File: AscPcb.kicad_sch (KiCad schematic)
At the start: 30 parts, among them J1 USB_C_Receptacle_USB2.0_16P, J2 B2B-PH-K-S, SW1 RESET, SW2 BOOT, U1 TLV75801PDRV, U2 BQ24040DSQR, U3 ESP32-C3-WROOM-02

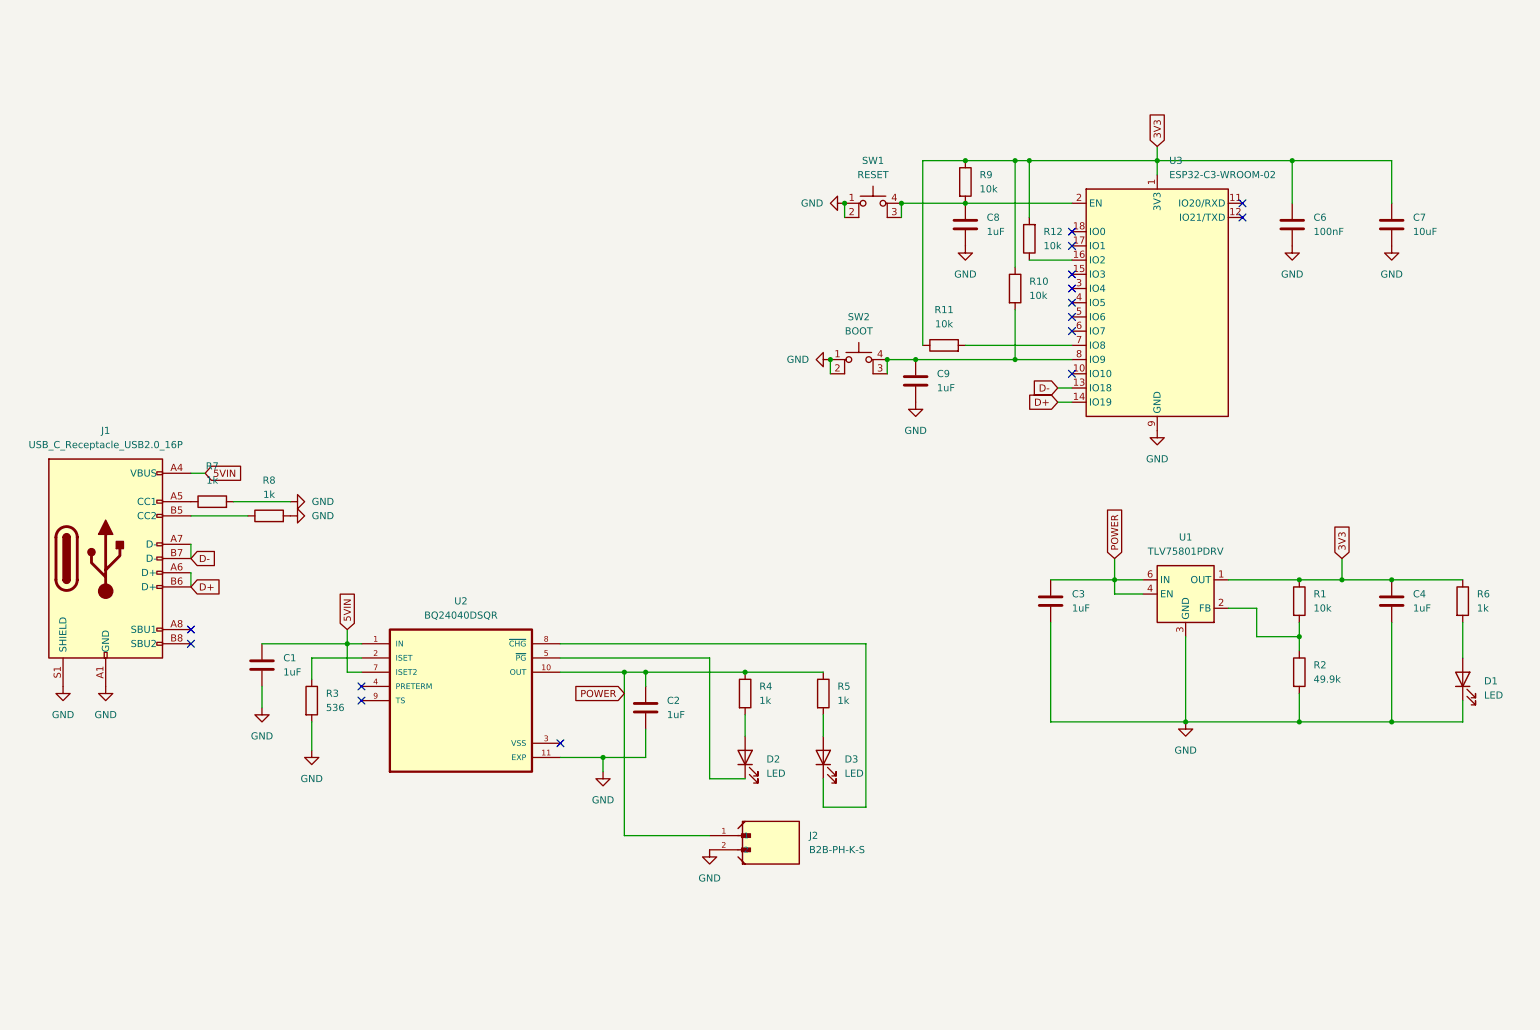
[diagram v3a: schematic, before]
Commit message: add more actual parts and add datasheets and MPNs
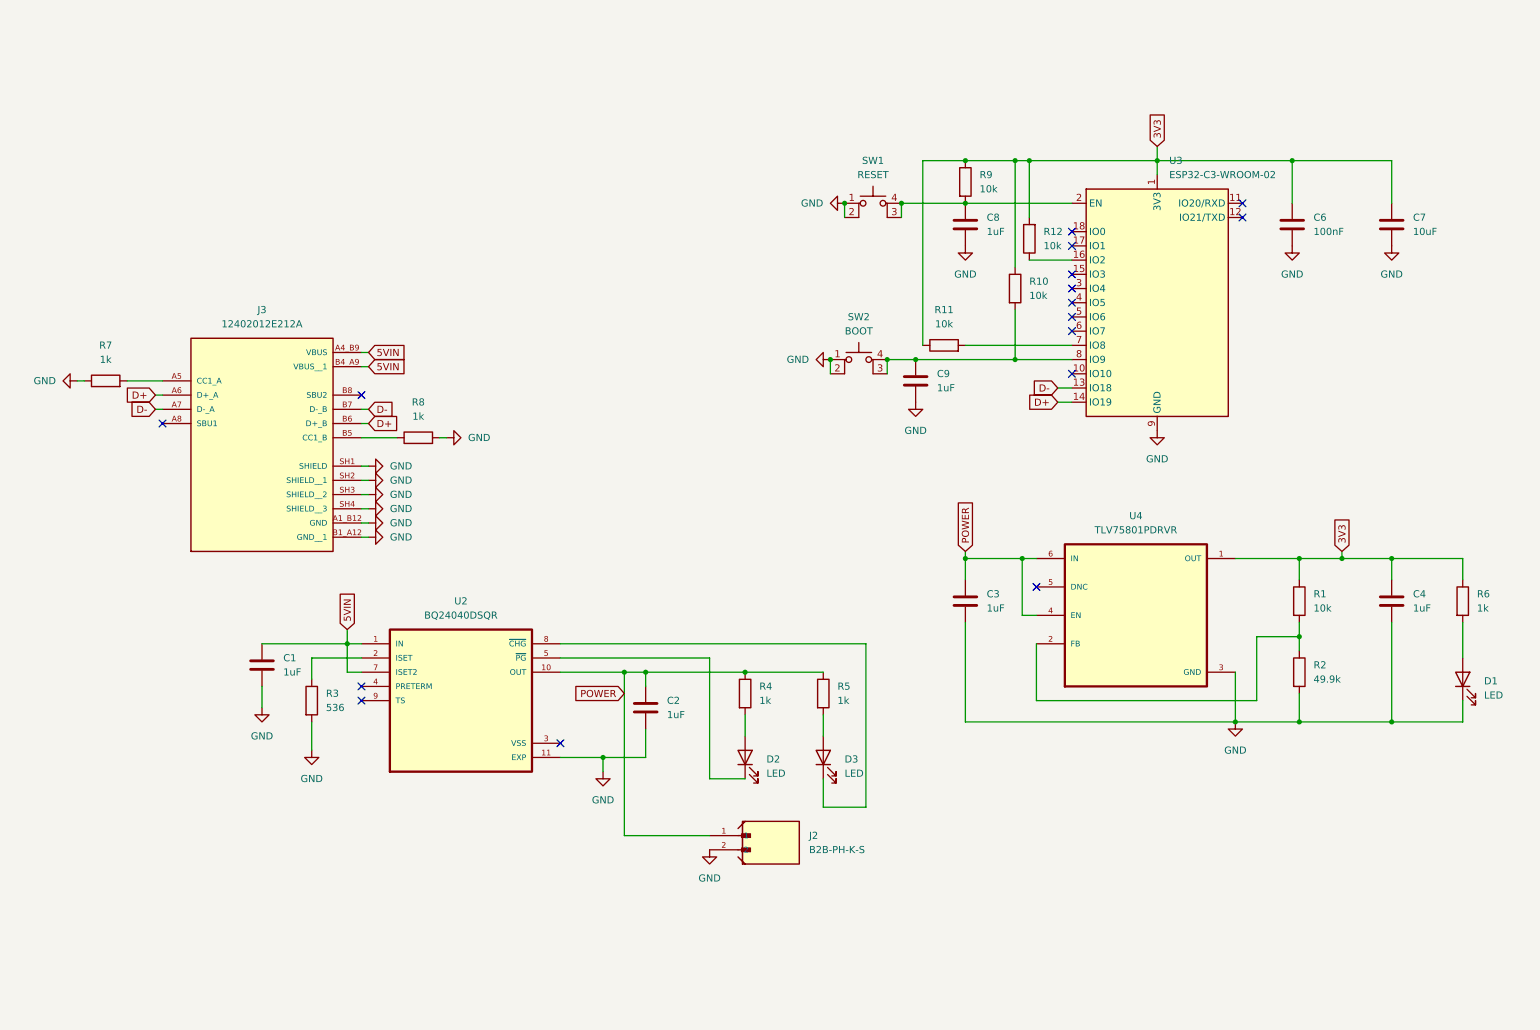
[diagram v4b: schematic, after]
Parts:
- removed J1: USB_C_Receptacle_USB2.0_16P, symbol Connector:USB_C_Receptacle_USB2.0_16P
- removed U1: TLV75801PDRV, Package_SON:WSON-6-1EP_2x2mm_P0.65mm_EP1x1.6mm, symbol Regulator_Linear:TLV75801PDRV
- added J3: 12402012E212A, 12402012E212A:AMPHENOL_12402012E212A, symbol 12402012E212A:12402012E212A
- added U4: TLV75801PDRVR, TLV75801PDRVR:SON65P200X200X80-7N, symbol TLV75801PDRVR:TLV75801PDRVR
- J2: MPN (none) -> B2B-PH-K-S
- U2: MPN (none) -> BQ24040DSQR
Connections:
- net 3V3: now also U4.1 (OUT)
- net 5VIN: now also J3.A4_B9 (VBUS), J3.B4_A9 (VBUS__1)
- net D+: now also J3.A6 (D+_A), J3.B6 (D+_B)
- net D-: now also J3.A7 (D-_A), J3.B7 (D-_B)
- net GND: now also R7.1, J3.A1_B12 (GND), J3.B1_A12 (GND__1), J3.SH1 (SHIELD), J3.SH2 (SHIELD__1), J3.SH3 (SHIELD__2), J3.SH4 (SHIELD__3), U4.3 (GND); no longer R7.2
- net POWER: now also U4.4 (EN), U4.6 (IN)
- net at R1.2, R2.1: now also U4.2 (FB)
- net at R8.1: now also J3.B5 (CC1_B)
- new net: J3.A5 (CC1_A), R7.2
- no-connect marks 15 -> 16
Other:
- moved on the sheet: C3

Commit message: clean up and other stuff
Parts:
- renumbered C6 to C5, C7 to C6, C8 to C7, C9 to C8, R7 to R1, R8 to R2, U3 to U1, U4 to U3
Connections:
- net 3V3 renamed +3V3
- net 5VIN renamed +5V
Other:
- moved on the sheet: C5, C6

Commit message: LEDs with correct Resistors
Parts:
- removed R6: 1k, Resistor_SMD:R_0603_1608Metric, symbol Device:R
- added R8: 30, Resistor_SMD:R_0603_1608Metric, symbol Device:R
- D1, D2: value LED -> Green; MPN (none) -> L135-R625003500001
- D3: value LED -> RED; MPN (none) -> L135-G525003500000
- R4, R5: value 1k -> 30; MPN CRCW06031K00FKEA -> RCP0603B30R0GEA
- renumbered R1 to R6, R2 to R7
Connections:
- net +3V3: now also R8.1
- net at D1.2 (A): now also R8.2

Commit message: schematic done
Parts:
- removed D1, D2: Green, LED_SMD:LED_0603_1608Metric, symbol Device:LED
- removed D3: RED, LED_SMD:LED_0603_1608Metric, symbol Device:LED
- removed SW1: RESET, Button_Switch_SMD:SW_SPST_PTS810, symbol Switch:SW_MEC_5E
- removed SW2: BOOT, Button_Switch_SMD:SW_SPST_PTS810, symbol Switch:SW_MEC_5E
- added D2: RED, L135_G525003500000:LED_L135-G525003500000, symbol L135-G525003500000:L135-G525003500000
- added D3, D4: Green, L135_G525003500000:LED_L135-G525003500000, symbol L135-G525003500000:L135-G525003500000
- added J3: Conn_01x10_Pin, Connector_PinHeader_1.00mm:PinHeader_1x10_P1.00mm_Vertical, symbol Connector:Conn_01x10_Pin
- added SW1, SW2: TL3305AF260QG, TL3305AF260QG:SW_TL3305AF260QG, symbol TL3305AF260QG:TL3305AF260QG
- U1: value ESP32-C3-WROOM-02 -> ESP32-C3-WROOM-02-N4; MPN (none) -> ESP32-C3-WROOM-02-N4
- renumbered J3 to J1
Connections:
- net GND: now also D3.C, SW1.1, SW1.2, SW2.1, SW2.2
- net at R8.2: now also D3.A
- net at U2.5 (~{PG}): now also D4.C
- net at R4.2: now also D4.A
- net at C8.1, R10.2, U1.8 (IO9): now also SW2.3, SW2.4
- net at U2.8 (~{CHG}): now also D2.C
- net at R5.2: now also D2.A
- net IO10: now reaches U1.10 (IO10)
- net IO10: now also J3.8 (Pin_8)
- net IO20: now reaches U1.11 (IO20/RXD)
- net IO20: now also J3.9 (Pin_9)
- net IO21: now reaches U1.12 (IO21/TXD)
- net IO21: now also J3.10 (Pin_10)
- net IO3: now reaches U1.15 (IO3)
- net IO3: now also J3.3 (Pin_3)
- net IO1: now reaches U1.17 (IO1)
- net IO1: now also J3.2 (Pin_2)
- net IO0: now reaches U1.18 (IO0)
- net IO0: now also J3.1 (Pin_1)
- net at C7.1, R9.2, U1.2 (EN): now also SW1.3, SW1.4
- net IO4: now reaches U1.3 (IO4)
- net IO4: now also J3.4 (Pin_4)
- net IO5: now reaches U1.4 (IO5)
- net IO5: now also J3.5 (Pin_5)
- net IO6: now reaches U1.5 (IO6)
- net IO6: now also J3.6 (Pin_6)
- net IO7: now reaches U1.6 (IO7)
- net IO7: now also J3.7 (Pin_7)
- no-connect marks 16 -> 6
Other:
- moved on the sheet: C5, C6, C7, C8, R10, R11, R12, R9

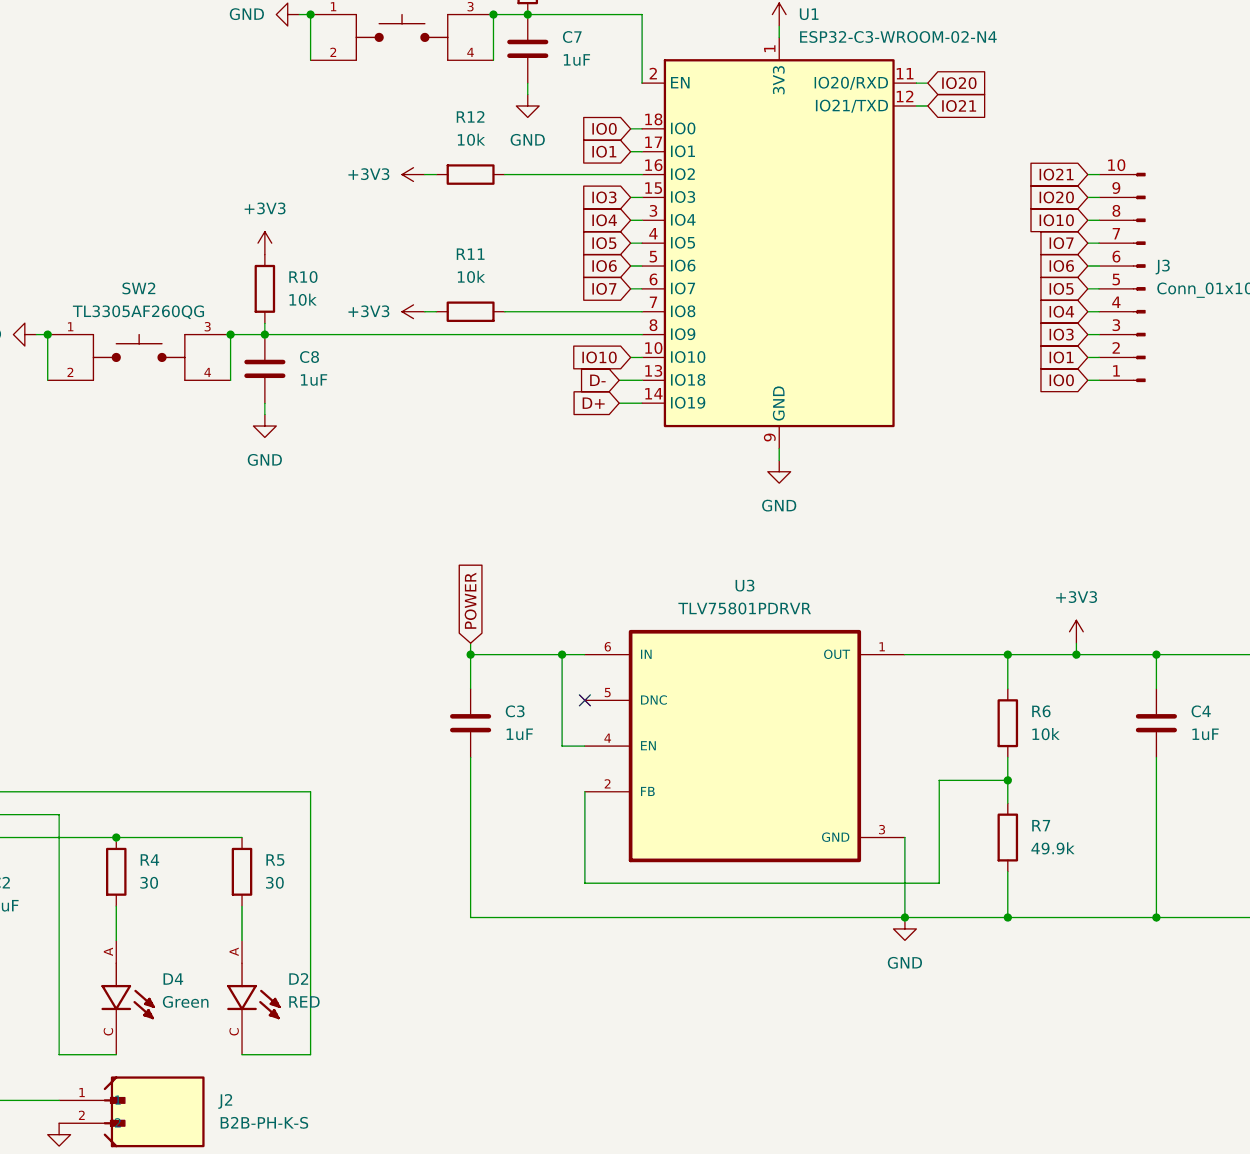
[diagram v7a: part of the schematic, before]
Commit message: sub circuits put together
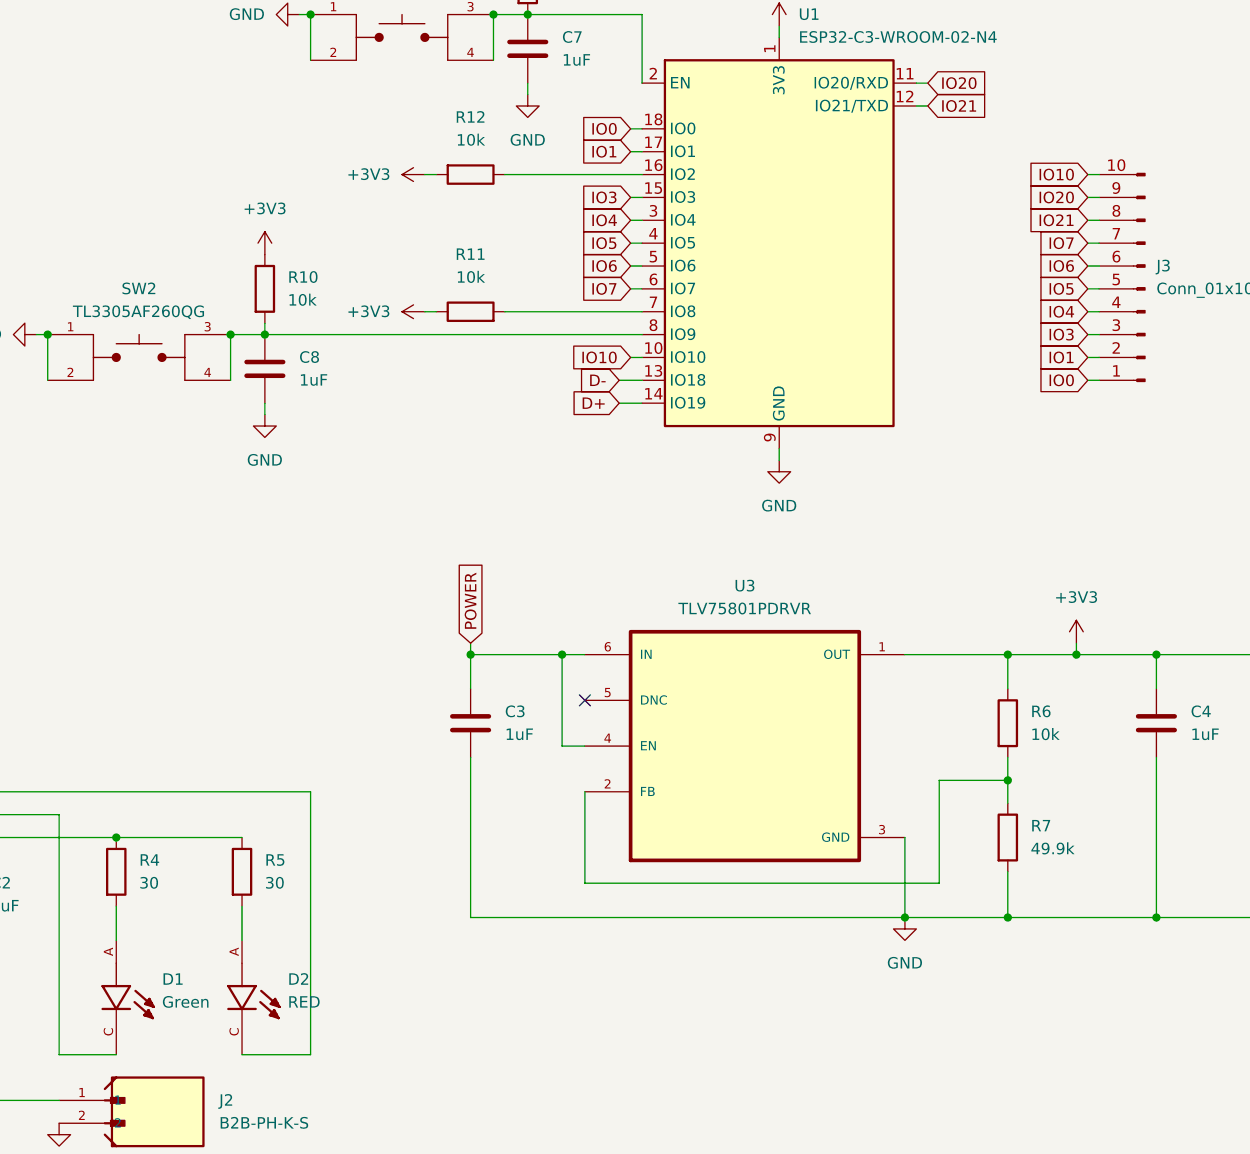
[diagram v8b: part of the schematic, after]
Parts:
- renumbered D4 to D1
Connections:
- net IO10: now also J3.10 (Pin_10); no longer J3.8 (Pin_8)
- net IO21: now also J3.8 (Pin_8); no longer J3.10 (Pin_10)
